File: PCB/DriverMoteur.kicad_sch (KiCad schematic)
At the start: 0 parts

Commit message: filled mototr driver schematic
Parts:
- added AC1: DRV8262DDVR, SOP64P810X120-44N, symbol SamacSys:DRV8262DDVR
- added C10, C11, C12: 100uF, CAPAE660X800N, symbol SamacSys_Parts:UCH1V101MCS1GS
- added C13, C7: 0.1uF/X7R, CAPC2012X94N, symbol SamacSys_Parts:0805DC104MAT2A
- added C8: 1uF, CAPC2012X94N, symbol SamacSys_Parts:0805DC104MAT2A
- added C9: 0.01 uF, CAPC2012X94N, symbol SamacSys_Parts:0805DC104MAT2A
- added J7, J8: 39501-1002, 395011002, symbol SamacSys:39501-1002
- added JP1, JP3: SolderJumper, Jumper:SolderJumper-3_P1.3mm_Bridged12_RoundedPad1.0x1.5mm, symbol Jumper:SolderJumper_3_Bridged12
- added JP2: SolderJumper_3_Open, symbol Jumper:SolderJumper_3_Open
- added R1, R3: 10k, symbol Device:R
- added R10, R4: ?, symbol Device:R
- added R12: NC, symbol Device:R
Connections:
- new net: AC1.23 (CPH), C7.1
- new net: AC1.24 (CPL), C7.2
- new net: AC1.40 (OCPM), R3.1
- new net: AC1.38 (MODE2), JP1.2 (C)
- new net 24V: AC1.11 (VM_2), AC1.12 (VM_3), AC1.2 (VM_1), AC1.21 (VM_4), C10.1 (+), C11.1 (+), C12.1 (+), C8.2, C9.1
- new net 3V3: AC1.33 (VREF1), AC1.34 (VREF2), AC1.42 (VCC), C13.2, JP1.1 (A), JP2.1 (A), JP3.1 (A), R1.2, R3.2
- new net CurrentSenseMotor1: AC1.36 (IPROPI1), R4.2
- new net CurrentSenseMotor2: AC1.37 (IPROPI2), R10.2
- new net DECAY: AC1.30 (DECAY), JP2.2 (C)
- new net GND: AC1.1 (GND_1), AC1.10 (GND_3), AC1.13 (GND_4), AC1.20 (GND_5), AC1.3 (GND_2), AC1.39 (MODE1), AC1.44 (GND_6), C10.2 (-), C11.2 (-), C12.2 (-), C13.1, C9.2, JP1.3 (B), JP2.3 (B), JP3.3 (B), R10.1, R12.1, R4.1
- new net IN1: AC1.26 (IN1)
- new net IN2: AC1.27 (IN2)
- new net IN3: AC1.28 (IN3)
- new net IN4: AC1.29 (IN4)
- new net Motor1_High: AC1.17 (OUT1_1), AC1.18 (OUT1_2), AC1.19 (OUT1_3), J7.1
- new net Motor1_Low: AC1.14 (OUT2_1), AC1.15 (OUT2_2), AC1.16 (OUT2_3), J7.2
- new net Motor2_High: AC1.4 (OUT3_1), AC1.5 (OUT3_2), AC1.6 (OUT3_3), J8.1
- new net Motor2_Low: AC1.7 (OUT4_1), AC1.8 (OUT4_2), AC1.9 (OUT4_3), J8.2
- new net NFAULT: AC1.41 (NFAULT), R1.1
- new net SLEEP: AC1.25 (NSLEEP)
- new net TOFF: AC1.32 (TOFF), JP3.2 (C), R12.2
- new net VCP: AC1.22 (VCP), C8.1
- no-connect marks 0 -> 3
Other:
- note added: "Default Configuration: OCPM = 1 --> Over Current Protection error = Retry MODE = 1 --> PWM mode Toff = 1 --> Waiting time between change = 16µs Decay = HZ --> Auto detect mode"
- note added: "Dépend du courant attendu A calculer! (page 21 datasheet)"

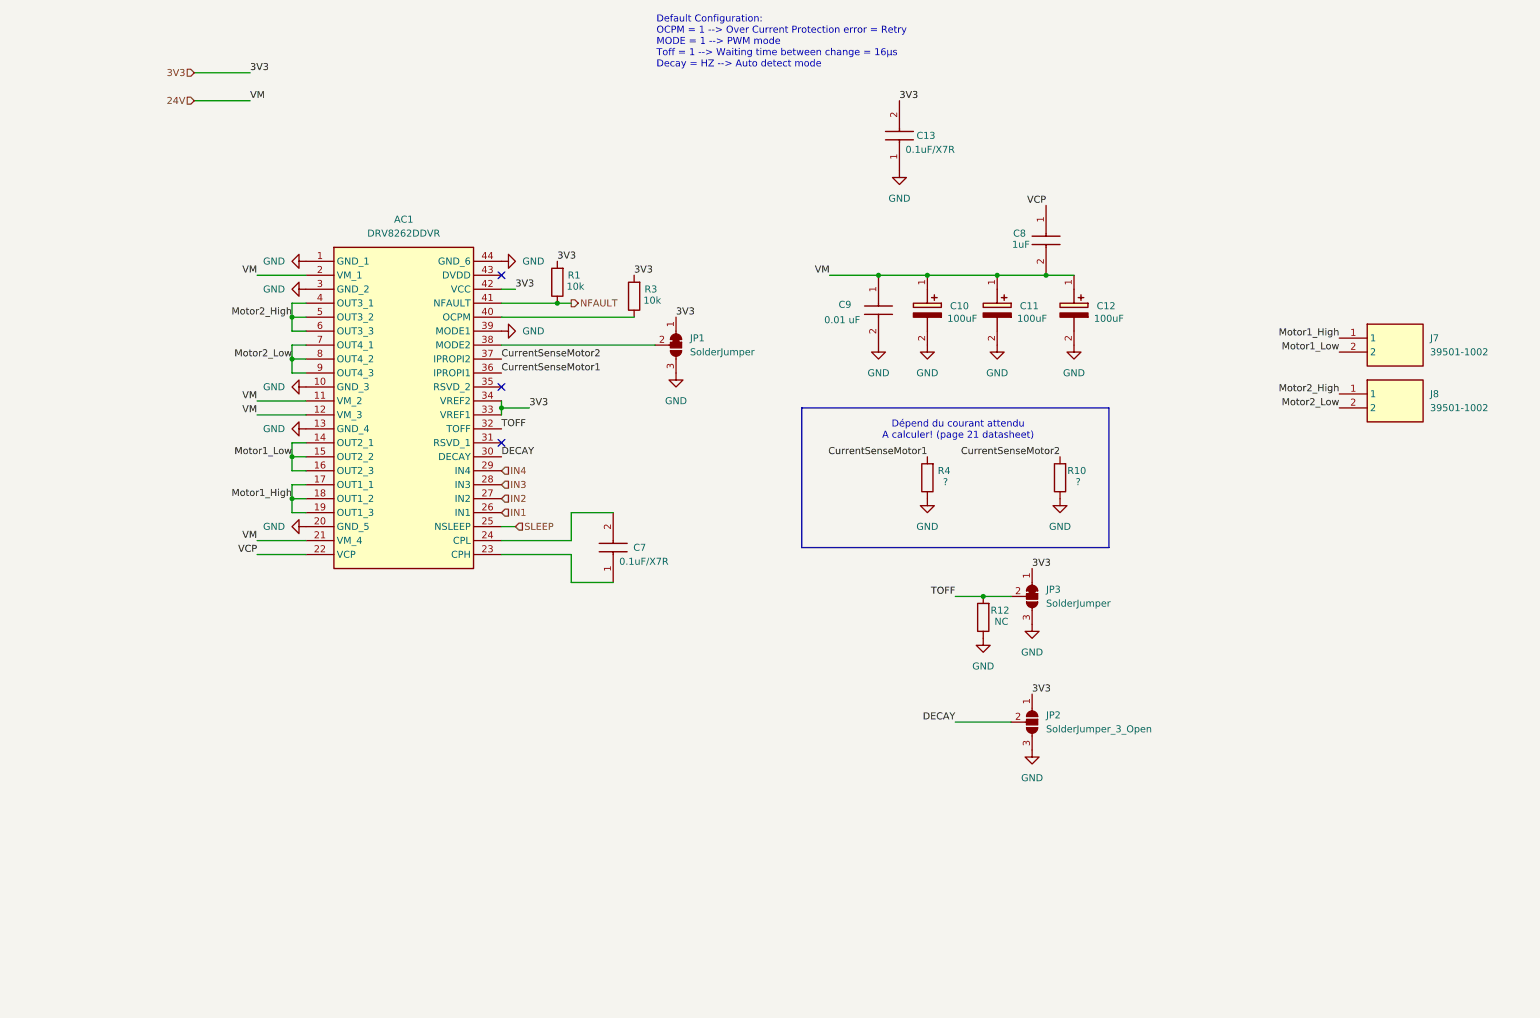
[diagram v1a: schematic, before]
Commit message: List of Modifs:
Corrected power supply sheet
Updated motor driver sheet
Added a project name to a lot of sheets (don't know why...)
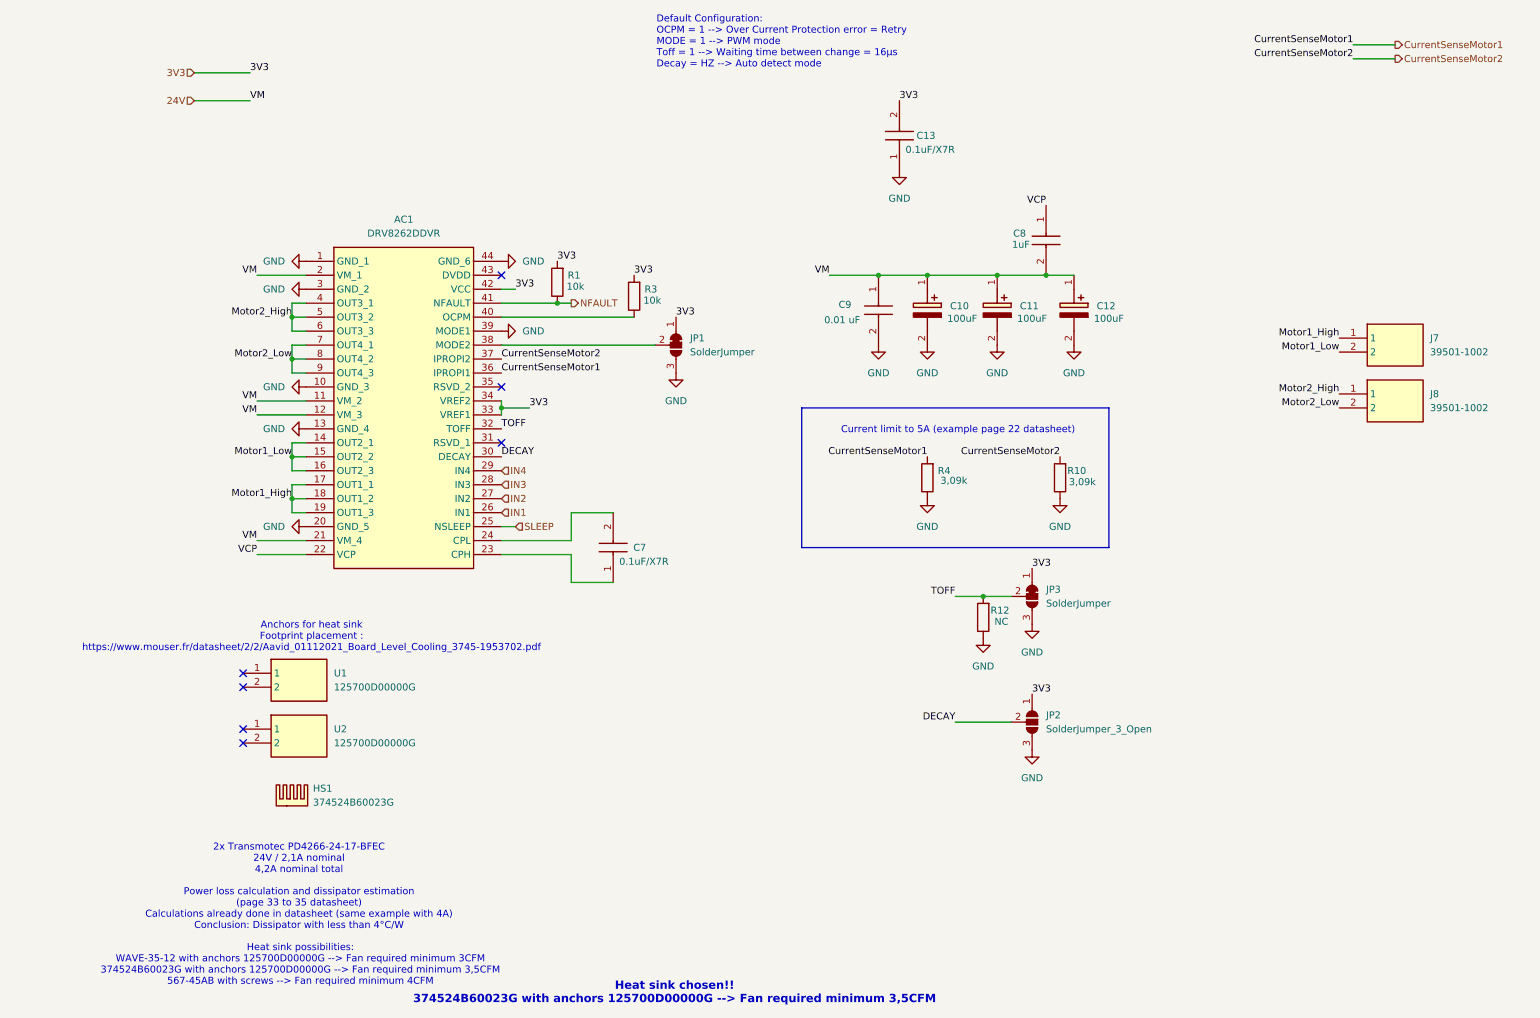
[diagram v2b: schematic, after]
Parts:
- added HS1: 374524B60023G, symbol Mechanical:Heatsink
- added U1, U2: 125700D00000G, 125700D00000G, symbol SamacSys_new:125700D00000G
- R10, R4: value ? -> 3,09k
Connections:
- no-connect marks 3 -> 7
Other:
- note added: "2x Transmotec PD4266-24-17-BFEC 24V / 2,1A nominal 4,2A nominal total"
- note added: "Anchors for heat sink Footprint placement : https://www.mouser.fr/datasheet/2/2/Aavid_01112021_Board_Level_Cooling_3745-1953702.pdf"
- note added: "Current limit to 5A (example page 22 datasheet)"
- note added: "Heat sink chosen!! 374524B60023G with anchors 125700D00000G --> Fan required minimum 3,5CFM"
- note added: "Heat sink possibilities: WAVE-35-12 with anchors 125700D00000G --> Fan required minimum 3CFM 374524B60023G with anchors 125700D00000G --> Fan required minimum 3,5CFM 567-45AB with screws --> Fan required minimum 4CFM"
- note added: "Power loss calculation and dissipator estimation (page 33 to 35 datasheet) Calculations already done in datasheet (same example with 4A) Conclusion: Dissipator with less than 4°C/W"
- note removed: "Dépend du courant attendu A calculer! (page 21 datasheet)"

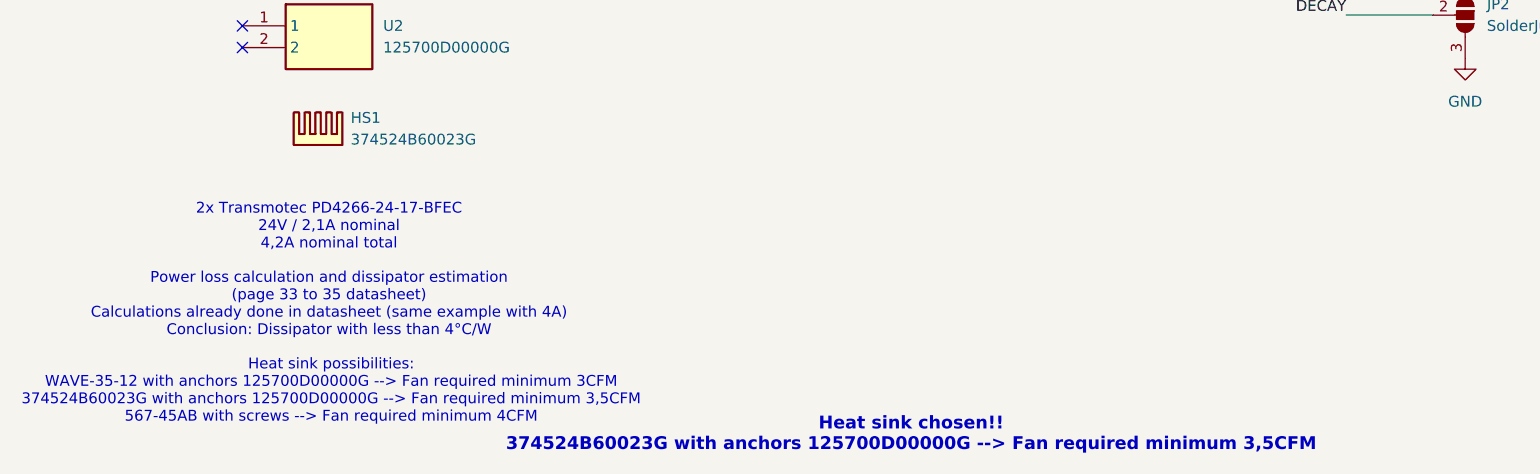
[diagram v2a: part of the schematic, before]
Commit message: ADD supplies to UC
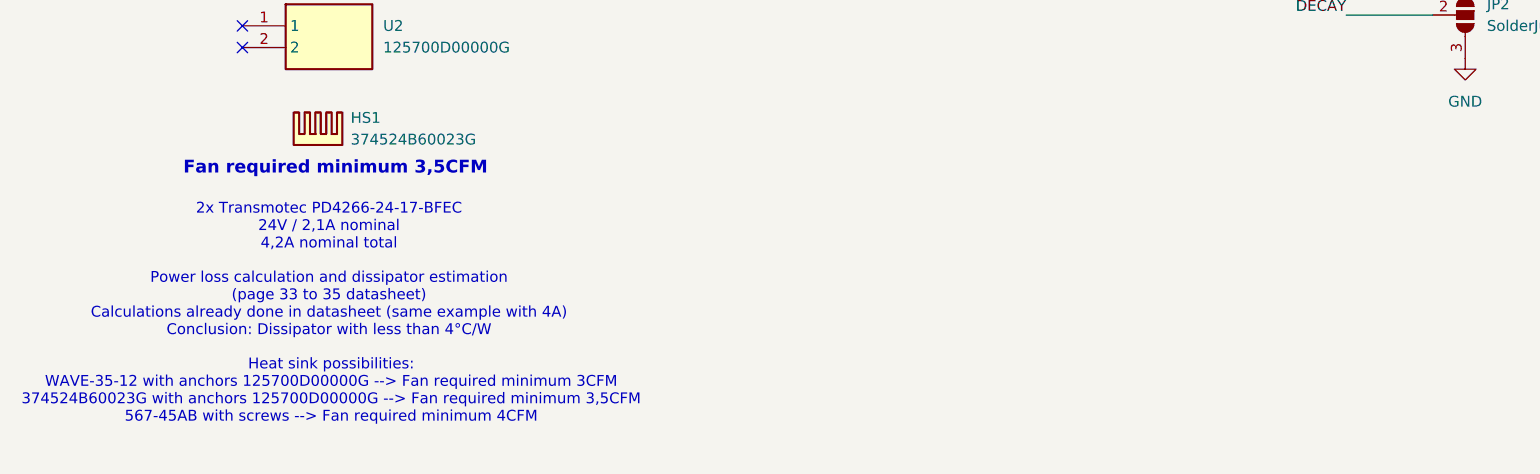
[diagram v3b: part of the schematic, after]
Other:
- note added: "Fan required minimum 3,5CFM"
- note removed: "Heat sink chosen!! 374524B60023G with anchors 125700D00000G --> Fan required minimum 3,5CFM"
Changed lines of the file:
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@@
-		)
-	)
-	(text "Heat sink chosen!!\n374524B60023G with anchors 125700D00000G --> Fan required minimum 3,5CFM"
-		(exclude_from_sim no)
-		(at 125.476 194.056 0)
-		(effects
-			(font
-				(size 1.5 1.5)
-				(thickness 0.4)
-				(bold yes)
-			)
 		)
 	)
@@
 			)
 		)
+	)
+	(text "Fan required minimum 3,5CFM"
+		(exclude_from_sim no)
+		(at 57.912 162.814 0)
+		(effects
+			(font
+				(size 1.5 1.5)
+				(thickness 0.4)
+				(bold yes)
+			)
+		)
